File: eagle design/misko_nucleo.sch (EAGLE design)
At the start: 12 parts, among them U1 ESQ-119-24-T-D

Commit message: - removed arduino connectors from lib
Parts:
- removed TP10, TP9: TPPAD1-17, testpad:TPPAD1-17
- removed U1: ESQ-119-24-T-D, NUCLEO:NUCLEO-L053R8
- added C1: 18pF, rcl:C-EUC0805
- added C10, C14, C15, C9: 1µF, rcl:C-EUC0805
- added C11: 22µF, rcl:C-EUC0805
- added C12, C8: 7pF, resistor:C-EUC0805
- added C13, C20, C3, C41, C42: 0.1µF, resistor:C-EUC0805
- added C16, C29, C34, C6: 10µF, rcl:C-EUC0805
- added C17: 2.2µF / 25V, rcl:C-EUC0805
- added C18: 1nF, rcl:C-EUC0805
- added C19, C21, C32, C36, C4, C43, C45: 0.1µF, rcl:C-EUC0805
- added C2: 1µF, resistor:C-EUC0805
- added C23, C37, C5: 10µF, resistor:C-EUC0805
- added C25: 1.5F, EECS5R5H155 Supercap:EECS5R5H155
- added C27, C30, C31, C35, C38: 1000µF, rcl:CPOL-EUE5-10.5
- added C39, C40: 100µF, rcl:C-EUC0805
- added C7: 18pF, resistor:C-EUC0805
- added CONN1: JTAG, JTAG 1.27mm 10pin header:JTAG-1.27-10-PIN-HEADER
- added CONN2: I2C, jumper:JP4E
- added CONN3: LiPo Battery, SIM800C:JST_2PIN-THM-RA
- added CONN4: USB mini B, MX-67503-1230 USB Mini-B SMT straight socket:MX-67503-1230
- added D1: 1N4148, Diode2:1N4148
- added D2: BAT60AE6327, diode:BAT60J
- added D4: SZ1SMB5916BT3G, diode:DIODE-SMB
- added D7: BZG05C3V6-E3-TR3, zener:ZENER
- added F1: PTS120615V050, SparkFun-Fuses:PPTC_THREE-QUARTER-AMP
- added IC1: ATMEGA1281-16AU, Atmel_By_element14_Batch_1-00:ATMEGA1281-16AU
- added IC10: ORG1510-MK4, ORG1510-MK4 GPS module:ORG1510-MK4
- added IC11: TPS3808G33DBVT, Texas Instruments_By_element14_Batch_1:TPS3808G33DBVT
- added IC12: LTC4425, LTC4425 Supercap Charger:LTC4425
- added IC13: RN4678_BT_MODULE, RN4678 Bluetooth 4.2 Dual Mode:RN4678_BT_MODULE
- added IC14: ADXL345, ADXL345 Accelerometer:ADXL345
- added IC15: 74HCT1G32, 74HCT1G32GW:74HCT1G32GW-DC
- added IC16: FM25W256-SOIC, FM25W256 FERAM:FM25W256-SOIC
- added IC17: MICROSD_SPI_MODE, Molex SD-47309 SD Card Slot:MICROSD_SPI_MODE
- added IC18: FH12-30S-0.5SH, con-hirose:FH12-30S-0.5SH
- added IC19: DS1394U-33+, DS1394U-33+ RTC SPI Module:DS1394U-33+
- added IC2: MC1525TT, microchip:MC1525TT
- added IC23: SP3012-04UTG, SP3012 TVS Diode Array:SP3012-04UTG
- added IC3: TMP36GRTZ, TMP36GRTZ:TMP36GRTZ-REEL7
- added IC4: TPS63031, TPS63031 - Buck Boost Voltage Regulator:TPS63001DRCR
- added IC5: MCP73871-2AAI/ML, MCP73871 - Powerpath and Charge Controller:MCP73871-2AAI/ML
- added IC6: MAX6818, MAX6818 CMOS Switch debouncer:MAX6818
- added IC7: FT230XS, ftdichip:FT230XS
- added IC8: SN74LVC1G3157DBVR - BT switch, Texas Instruments_By_element14_Batch_1:SN74LVC1G3157DBVR
- added IC9: SN74LVC1G3157DBVR - GPS switch, Texas Instruments_By_element14_Batch_1:SN74LVC1G3157DBVR
- added L1: DL0805-33 33µH, rcl:L-US
- added L2: DJNR3015-1R5, DJNR3015-1R5 Inductor:DJNR3015-1R5
- added LED1: TX, led:LEDCHIPLED_1206
- added LED2: RX, led:LEDCHIPLED_1206
- added LED3: green, led:LEDSQR2X5
- added LED4: red, led:LEDSQR2X5
- added MISKO: misko, NUCLEO-H503RB-B02:NUCLEO-H503RB-B02
- added Q1: ABM3B-8MHZ-10-1-U-T, ABM3B-8MHZ-10-1-U-T - Quartz Resonator:ABM3B
- added Q2: LFXTAL016178R, LFXTAL016178R 32.768kHz crystal:LFXTAL016178R
- added R1, R16, R20, R25: 47k, rcl:R-EU_R0805
- added R10, R6: 27, resistor:R-EU_R0805
- added R12, R37: 100k, rcl:R-EU_R0805
- added R13, R39: 270k, rcl:R-EU_R0805
- added R14, R15, R22, R30, R35: 1k, resistor:R-EU_R0805
- added R17, R18, R33, R34: 1k, rcl:R-EU_R0805
- added R19, R32, R41, R9: 10k, rcl:R-EU_R0805
- added R2, R23, R27, R28, R36, R42, R43: 10k, resistor:R-EU_R0805
- added R26: 390k, rcl:R-EU_R0805
- added R29: 1M, resistor:R-EU_R0805
- added R3: 4k7, rcl:R-EU_R0805
- added R4, R5: 3k3, rcl:R-EU_R0805
- added R40: NTC 10k, rcl:R-EU_0204/5
- added R44, R45, R7, R8: 150k, rcl:R-EU_R0805
- added R46, R47: 470k, resistor:R-EU_R0805
- added SJ3: RESET, jumper:SJW
- added SW1: RESET, Wurth_Elektronik_Electromechanic_Switch_rev17c:430152050836
- added SW2: POWER SWITCH, smd-special:SWS001
- added SW3: MICROJOYSTICK, micro joystick:MICROJOYSTICK
- added SW4, SW5: PB6156RSL, PB6156RSL Illuminated Tact SPST-NO switch:PB6156RSL
- added T1: BSS84, transistor-small-signal:BSS84
- TP1, TP2, TP3: value TPPAD1-17 -> GND; device testpad:TPPAD1-17 -> testpad:TPPAD1-17Y
- TP11: value TPPAD1-17 -> Bluetooth Wakeup Pin; device testpad:TPPAD1-17 -> testpad:PTR1TP14R
- TP4: value TPPAD1-17 -> VCC; device testpad:TPPAD1-17 -> testpad:PTR1TP14R
- TP5: value TPPAD1-17 -> VLiIon Regulated; device testpad:TPPAD1-17 -> testpad:PTR1TP14R
- TP6: value TPPAD1-17 -> VGPS; device testpad:TPPAD1-17 -> testpad:PTR1TP14R
- TP7: value TPPAD1-17 -> Analogue Switch CRTL Pin; device testpad:TPPAD1-17 -> testpad:PTR1TP14R
- TP8: value TPPAD1-17 -> GPS Power CTRL Pin; device testpad:TPPAD1-17 -> testpad:PTR1B1,27
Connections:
- removed net 3V3: TP1.TP, TP7.TP, U1G$3.+3V3
- removed net AB-RTC_!INT!: TP6.TP
- removed net ANAL.SW.CTRL.: TP5.TP
- removed net EXTI_ADXL345: TP6.TP, U1G$6.PB4
- removed net EXTI_PUSHBUTTON: U1G$3.PC13
- removed net GPS_ON: TP1.TP
- removed net INT_AB-RTC: TP11.TP
- removed net LED_GREEN: U1G$3.PC10
- removed net LED_RED: U1G$3.PC11
- removed net N$2: TP4.TP
- removed net N$67: U1G$3.PA15
- removed net N$70: U1G$3.BOOT0
- removed net N$71: U1G$3.VDD
- removed net N$72: U1G$3.PC12
- removed net RCC_OSC_IN: U1G$3.PH0
- removed net SPI1_MISO: U1G$6.PA6
- removed net SPI1_MOSI: U1G$6.PA7
- removed net SPI1_SCK: U1G$6.PA5
- removed net SPI1_SS_ADXL345: U1G$6.PB6
- removed net SPI1_SS_MR25H256: U1G$6.PC7
- removed net SWCLK: U1G$3.PA14
- removed net SWDIO: U1G$3.PA13
- removed net USART2_RX: U1G$6.PA3
- removed net USART2_TX: U1G$6.PA2
- removed net USART3_RX: U1G$6.PB11
- removed net USART3_TX: U1G$6.PB10
- removed net USB_DM: U1G$6.PA11
- removed net USB_DP: U1G$6.PA12
- removed net VIN: TP9.TP, U1G$3.VIN
- removed net _AB-RTC_CLKOUT: TP5.TP
- removed net _GPS_1PPS: TP3.TP
- new net ADXL345SDA: IC14.SDA, IC15.Y
- new net ADXL345_INT1_INTERRUPT_PIN: CONN2.3, IC1.(SCL/INT0)_PD0, IC14.INT1
- new net ANALOG_SW_CTRL_PIN: IC1.PA7_(AD7), IC8.S, IC9.S, TP7.TP
- new net AREF: C5.1, IC1.AREF, IC2.VO
- new net AVCC: C41.2, IC1.AVCC, IC2.VIN, L1.2
- new net BAT_A_PIN: IC1.PF2_(ADC2), R44.2, R45.1
- new net BLUETOOTH_PROF_IND_PIN: IC1.PG2_(ALE), IC13.P0_5, TP11.TP
- new net BLUETOOTH_RX: IC13.RXD, IC8.A
- new net BLUETOOTH_SWITCH_PIN: IC1.PC6_(A14), IC13.SW_BTN, R43.2
- new net BLUETOOTH_TX: IC13.TXD, IC9.B1
- new net BLUETOOTH_WAKEUP_PIN: IC1.PC7_(A15), IC13.WAKEUP, R42.2
- new net BT_LED: IC13.LED, R22.1
- new net BUTTON_BLUETOOTH: IC6.IN7, SW4.3
- new net BUTTON_CENTER: IC6.IN5, SW3.CENTER
- new net BUTTON_DOWN: IC6.IN2, SW3.DOWN
- new net BUTTON_GPRS: IC6.IN8, SW5.3
- new net BUTTON_LEFT: IC6.IN4, SW3.LEFT
- new net BUTTON_RIGHT: IC6.IN3, SW3.RIGHT
- new net BUTTON_UP: IC6.IN6, SW3.UP
- new net CAP1N: C9.1, IC18-5.1
- new net CAP1P: C9.2, IC18-4.1
- new net CAP2N: C10.1, IC18-3.1
- new net CAP2P: C10.2, IC18-2.1
- new net CBUS1: IC7.CBUS1, LED2.C
- new net CBUS2: IC7.CBUS2, LED1.C
- new net D+: CONN4.D+, IC23.4
- new net D-: CONN4.D-, IC23.2
- new net EN: IC4.EN, R2.2, SW2.1
- new net GPRS_NETLIGHT: R27.1, R28.1
- new net GPRS_NETLIGHT_GATE: R28.2, T1.G
- new net GPS_GREEN_LED_PIN: IC1.PA3_(AD3), R17.1
- new net GPS_ON_OFF: IC10.ON_OFF, IC11.~RESET, R29.1
- new net GPS_POWER_CTL_PIN: IC1.PA6_(AD6), IC11.~MR, R23.1, TP8.TP
- new net GPS_RED_LED_PIN: IC1.PA4_(AD4), R18.1
- new net GPS_SW_SERIAL_RX: IC1.(OC2A/_PCINT4)_PB4, IC8.B2, IC9.A
- new net GPS_SW_SERIAL_TX: C7.2, IC1.(OC1A/PCINT5)_PB5, IC10.RX, IC8.B1
- new net GPS_TX: C1.1, IC10.TX, IC9.B2
- new net GPS_WAKEUP_PIN: IC1.PA5_(AD5), IC10.WAKEUP
- new net GREEN_LED: LED3.C, R17.2
- new net ID: CONN4.ID, IC23.5
- new net IREF: IC18-26.1, R26.2
- new net JTAG_TCL_PIN: CONN1.TCK, IC1.PF4_(ADC4/TCK)
- new net JTAG_TDI_PIN: CONN1.TDI, IC1.PF7_(ADC7/TDI)
- new net JTAG_TDO_PIN: CONN1.TDO, IC1.PF6_(ADC6/TDO)
- new net JTAG_TMS_PIN: CONN1.TMS, IC1.PF5_(ADC5/TMS)
- new net L2: R22.2, SW4.L2
- new net LDO33_O: IC13.LDO33_O, IC13.VDD_IO, SW4.L1
- new net LTC4425_EN: IC12.EN, R35.2
- new net LTC4425_PROG: IC12.PROG, R36.2
- new net L_L1: IC4.L1, L2.L1
- new net L_L2: IC4.L2, L2.L2
- new net MCP73871_CHARGE_STATUS_1_PIN: IC1.PA0_(AD0), IC5.STAT1/!LBO!, R25.2
- new net MCP73871_CHARGE_STATUS_2_PIN: IC1.PA1_(AD1), IC5.STAT2, R20.2
- new net MCP73871_POWER_GOOD_PIN: IC1.PA2_(AD2), IC5.!PG!, R16.2
- new net MENU_BLUETOOTH_POWER_BUTTON_PIN: IC1.PC4_(A12), IC6.OUT7
- new net MENU_CENTER_BUTTON_PIN: IC1.PC2_(A10), IC6.OUT5
- new net MENU_DOWN_BUTTON_PIN: IC1.PG1_(~RD), IC6.OUT2
- new net MENU_GPRS_POWER_BUTTON_PIN: IC1.PC5_(A13), IC6.OUT8
- new net MENU_LEFT_BUTTON_PIN: IC1.PC1_(A9), IC6.OUT4
- new net MENU_RIGHT_BUTTON_PIN: IC1.PC0_(A8), IC6.OUT3
- new net MENU_UP_BUTTON_PIN: IC1.PC3_(A11), IC6.OUT6
- new net N$12: MISKOCN7.5V0
- new net N$13: MISKOCN7.IOREF
- new net N$15: MISKOCN7.NRST
- new net N$16: MISKOCN7.BOOT0
- new net N$21: MISKOCN7.PD2
- new net N$22: MISKOCN7.PC15
- new net N$26: MISKOCN7.PC11
- new net N$27: MISKOCN7.PC10
- new net N$28: MISKOCN7.PC3
- new net N$31: C3.2, D1.A, R1.1
- new net N$32: MISKOCN7.PC0
- new net N$33: MISKOCN7.PB0
- new net N$34: MISKOCN7.PA15
- new net N$35: MISKOCN7.PA14
- new net N$4: F1.2, IC23.1
- new net N$46: MISKOCN10.PC8
- new net N$47: MISKOCN10.PC9
- new net N$48: MISKOCN10.AGND
- new net N$49: MISKOCN10.GND
- new net N$50: MISKOCN10.PA5
- new net N$53: MISKOCN10.PA10
- new net N$56: MISKOCN10.PB2
- new net N$6: C27.+, C30.+, C31.+, C35.+, C38.+, D2.C
- new net N$61: MISKOCN10.PB8
- new net N$64: MISKOCN10.PB13
- new net N$66: MISKOCN10.PB15
- new net PDI_UART0_CTS_PIN: IC1.(OC0B)_PG5, IC7.!CTS
- new net PDI_UART0_RX_PIN: IC1.(RXD0/PCINT8/PDI)_PE0, R4.1
- new net PDI_UART0_TX_PIN: IC1.(TXD0/PDO)_PE1, R5.1
- new net PFI: IC12.PFI, R46.1, R47.2
- new net PFI_RET: IC12.PFI_RET, R47.1
- new net PROG1: IC5.PROG1, R34.1
- new net PROG3: IC5.PROG3, R37.1
- new net RED_LED: LED4.C, R18.2
- new net RESET: CONN1.RESET, IC1.~RESET, R1.2, R3.2, SW1.2, SW1.4
- new net RTC_INT_INTERRUPT_PIN: CONN2.4, IC1.(SDA/INT1)_PD1, IC19.!INT!
- new net RTC_XTAL1: IC19.X1, Q2.XTAL1
- new net RTC_XTAL2: IC19.X2, Q2.XTAL2
- new net RXD: IC7.RXD, R5.2
- new net SD_CARD_DETECT_PIN: IC1.(XCK0/AIN0)_PE2, IC17.CARD_DETECT
- new net SPI_MISO_PIN: IC1.(MISO/PCINT3)_PB3, IC14.SDO, IC16.SO, IC17.DO, IC19.DOUT
- new net SPI_MOSI_PIN: IC1.(MOSI/PCINT2)_PB2, IC15.B, IC16.SI, IC17.DI, IC18-19.1, IC19.DIN
- new net SPI_OLED_D/C_PIN: IC1.(OC0A/OC1C/PCINT7)_PB7, IC18-15.1
- new net SPI_OLED_RESET_PIN: IC1.(TOSC2)_PG3, IC18-14.1
- new net SPI_SCK_PIN: IC1.(SCK/PCINT1)_PB1, IC14.SCL, IC16.SCK, IC17.CLK, IC18-18.1, IC19.SCLK
- new net SPI_SS_ADXL345_PIN: IC1.(OC1B/PCINT6)_PB6, IC14.!CS!, IC15.A, R9.2
- new net SPI_SS_FRAM_PIN: IC1.(~SS/PCINT0)_PB0, IC16.!CS!, R19.1
- new net SPI_SS_OLED_PIN: IC1.(TOSC1)_PG4, IC18-13.1
- new net SPI_SS_RTC_PIN: IC1.(OC3C/INT5)_PE5, IC19.!CS!, R32.2
- new net SPI_SS_SD_CARD_PIN: IC1.(OC3A/AIN1)_PE3, IC17.CS, R41.1
- new net THERM: IC5.THERM, R33.1
- new net TMP36_VSENSE_PIN: IC1.PF3_(ADC3), IC3.VOUT
- new net TXD: IC7.TXD, R4.2
- new net UART1_GPS_RX: IC1.(RXD1/INT2)_PD2
- new net UART1_GPS_TX: IC1.(TXD1/INT3)_PD3
- new net USBDM: IC7.USBDM, R10.1
- new net USBDP: IC7.USBDP, R6.2
- new net USB_D+: IC23.7, R6.1
- new net USB_D-: IC23.9, R10.2
- new net USB_ID: IC23.6
- new net USB_RX_LED: LED1.A, R14.2
- new net USB_TX_LED: LED2.A, R15.2
- new net VCC: C11.2, C14.2, C15.2, C16.2, C19.2, C20.1, C21.1, C29.1, C32.1, C34.1, C36.1, C4.1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
- new net VCC_SENSE_PIN: IC1.PF1_(ADC1), R7.2, R8.1
- new net VCOMH: C17.2, IC18-27.1
- new net VGPS: C18.1, C2.1, C25.+, C39.1, IC10.VCC, IC11.SENSE, IC12.VOUT1, IC12.VOUT2, IC19.VBACK, TP6.TP
- new net VMID: C39.2, C40.2, IC12.VMID
- new net VPCC: IC5.VPCC, R12.2, R13.1
- new net VUSB: CONN4.VBUS, F1.1, R14.1, R15.1, TP2.TP
- new net V_LIION+: C37.1, CONN3.2, IC5.VBAT1, IC5.VBAT2, IC5.VBAT_SENSE, R44.1
- new net V_LIION_REGULATED: C23.1, C45.1, C6.2, IC4.PS/SYNC, IC4.VIN, IC4.VINA, IC5.OUT1, IC5.OUT2, SW2.2, SW5.L1, TP5.TP
- new net XTAL1: C12.2, IC1.XTAL1, Q1.Q2
- new net XTAL2: C8.2, IC1.XTAL2, Q1.Q1
- net 5V0: now also C42.2, D2.A, IC23.10, IC5.!TE!, IC5.CE, IC5.IN1, IC5.IN2, IC5.PROG2, IC5.SEL, IC7.VCC, R12.1; no longer TP8.TP, U1G$3.+5V
- net GND: now also C1.2, C11.1, C12.1, C13.2, C14.1, C15.1, C16.1, C17.1, C18.2, C19.1, C2.2, C20.2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; no longer TP10.TP, U1G$3.GND_19, U1G$3.GND_20, U1G$3.GND_22, U1G$3.GND_8, U1G$6.GND_20, U1G$6.GND_9, U1G$7.GND_CN11_1, U1G$7.GND_CN11_2, U1G$7.GND_CN12_1, U1G$7.GND_CN12_2
- net N$1: now also R30.1, SW5.L2; no longer U1G$6.PC4
- net N$10: now also C13.1, IC7.!RESET, IC7.3V3OUT, IC7.VCCIO; no longer U1G$6.PB1
- net N$11: now also IC13.!RST_N!, SJ3.1; no longer U1G$6.PB2
- net N$14: now also MISKOCN7.3V3; no longer U1G$6.PB12
- net N$17: now also MISKOCN7.GND; no longer U1G$6.U5V
- net N$18: now also MISKOCN7.PF1; no longer U1G$6.PC5
- net N$19: now also R33.2, R39.1, R40.1; no longer U1G$6.PC6
- net N$20: now also MISKOCN7.PF0; no longer U1G$6.PC8
- net N$23: now also MISKOCN7.PC14; no longer U1G$6.PA10
- net N$24: now also MISKOCN7.PC13; no longer U1G$6.PB3
- net N$25: now also MISKOCN7.PC12; no longer U1G$6.PB5
- net N$29: now also MISKOCN7.PC2; no longer U1G$6.PA9
- net N$3: now also R30.2, T1.S; no longer TP3.TP
- net N$30: now also MISKOCN7.PC1; no longer U1G$6.PA8
- net N$36: now also MISKOCN7.PA13; no longer U1G$6.AVDD
- net N$37: now also MISKOCN7.PA2; no longer U1G$6.PB9
- net N$38: now also MISKOCN7.PA1; no longer U1G$6.PB8
- net N$39: now also MISKOCN7.PA0; no longer U1G$6.PC9
- net N$40: now also MISKOCN10.AVDD; no longer U1G$3.PC0
- net N$41: now also MISKOCN10.VBUS_STLK; no longer U1G$3.PC1
- net N$42: now also MISKOCN10.PC4; no longer U1G$3.PB0
- net N$43: now also MISKOCN10.PC5; no longer U1G$3.PA4
- net N$44: now also MISKOCN10.PC6; no longer U1G$3.PA1
- net N$45: now also MISKOCN10.PC7; no longer U1G$3.PA0
- net N$5: now also MISKOCN7.VBAT; no longer U1G$6.AGND
- net N$51: now also MISKOCN10.PA6; no longer U1G$3.RESET
- net N$52: now also MISKOCN10.PA7; no longer U1G$3.IOREF
- net N$54: now also MISKOCN10.PA8; no longer U1G$3.E5V
- net N$55: now also MISKOCN10.PB1; no longer U1G$3.PD2
- net N$57: now also MISKOCN10.PB4; no longer U1G$3.PC3
- net N$58: now also MISKOCN10.PB5; no longer U1G$3.PC2
- net N$59: now also MISKOCN10.PB6; no longer U1G$3.VLCD
- net N$60: now also MISKOCN10.PB7; no longer U1G$3.PH1
- net N$62: now also MISKOCN10.PB10; no longer U1G$3.PC15
- net N$63: now also MISKOCN10.PB12; no longer U1G$3.PC14
- net N$65: now also MISKOCN10.PB14; no longer U1G$3.PB7
- net N$7: now also MISKOCN7.VDD; no longer U1G$6.PB13
- net N$8: now also MISKOCN7.VIN; no longer U1G$6.PB14
- net N$9: now also MISKOCN7.E5V; no longer U1G$6.PB15
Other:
- note added: "ADXL345 Accelerometer"
- note added: "AVCC Circuit"
- note added: "Analog Switch"
- note added: "Bluetooth Module"
- note added: "Buttons"
- note added: "Debouncer"
- note added: "ER-OLED015-2W Connetor w. SSD1309"
- note added: "FERAM Module"
- note added: "GPS module"
- note added: "Joystick"
- note added: "Motherboard"
- note added: "OLED"
- note added: "Oscillator Circuit"
- note added: "Power Supply - Buck/Boost Regulator"
- note added: "Power Supply - Power Path Controller"
- note added: "RTC Clock"
- note added: "Reset Circuit"
- note added: "SD Card Slot"
- note added: "SPI Bus"
- note added: "Status LEDs"
- note added: "Supercap Charger"
- note added: "Temperature Sensor"
- note added: "USB connetor"
- note added: "USB to Serial"
- note added: "VGPS Voltage Supervisor"
- note added: "Vcc Measurement"
- note added: "Voltage Reference"
- note removed: "TODO: remove & hardwire"
- moved on the sheet: TP1, TP2, TP3

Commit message: - defined net classes, added power symbols, ground fill
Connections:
- net N$13 renamed IOREF
- net N$14 renamed 3V3
- net N$15 renamed NRST
- net N$16 renamed BOOT0
- net N$18 renamed PF1
- net N$20 renamed PF0
- net N$21 renamed PD2
- net N$22 renamed PC15
- net N$23 renamed PC14
- net N$24 renamed PC13
- net N$25 renamed PC12
- net N$26 renamed PC11
- net N$27 renamed PC10
- net N$28 renamed PC3
- net N$29 renamed PC2
- net N$30 renamed PC1
- net N$32 renamed PC0
- net N$33 renamed PB0
- net N$34 renamed PA15
- net N$35 renamed PA14
- net N$36 renamed PA13
- net N$37 renamed PA2
- net N$38 renamed PA1
- net N$39 renamed PA0
- net N$40 renamed AVDD
- net N$41 renamed VBUS_STLK
- net N$42 renamed PC4
- net N$43 renamed PC5
- net N$44 renamed PC6
- net N$45 renamed PC7
- net N$46 renamed PC8
- net N$47 renamed PC9
- net N$5 renamed VBAT
- net N$50 renamed PA5
- net N$51 renamed PA6
- net N$52 renamed PA7
- net N$53 renamed PA9
- net N$54 renamed PA8
- net N$55 renamed PB1
- net N$56 renamed PB2
- net N$57 renamed PB4
- net N$58 renamed PB5
- net N$59 renamed PB6
- net N$60 renamed PB7
- net N$61 renamed PB8
- net N$62 renamed PB10
- net N$63 renamed PN12
- net N$64 renamed PB13
- net N$65 renamed PB14
- net N$66 renamed PB15
- net N$7 renamed VDD
- net N$8 renamed VIN
- net N$9 renamed E5V
- removed net N$12: MISKOCN7.5V0
- removed net N$17: MISKOCN7.GND
- removed net N$48: MISKOCN10.AGND
- removed net N$49: MISKOCN10.GND
- new net OLD_5V0: C42.2, D2.A, IC23.10, IC5.!TE!, IC5.CE, IC5.IN1, IC5.IN2, IC5.PROG2, IC5.SEL, IC7.VCC, R12.1
- net 5V0: now also MISKOCN7.5V0; no longer C42.2, D2.A, IC23.10, IC5.!TE!, IC5.CE, IC5.IN1, IC5.IN2, IC5.PROG2, IC5.SEL, IC7.VCC, R12.1
- net GND: now also MISKOCN10.AGND, MISKOCN10.GND, MISKOCN7.GND

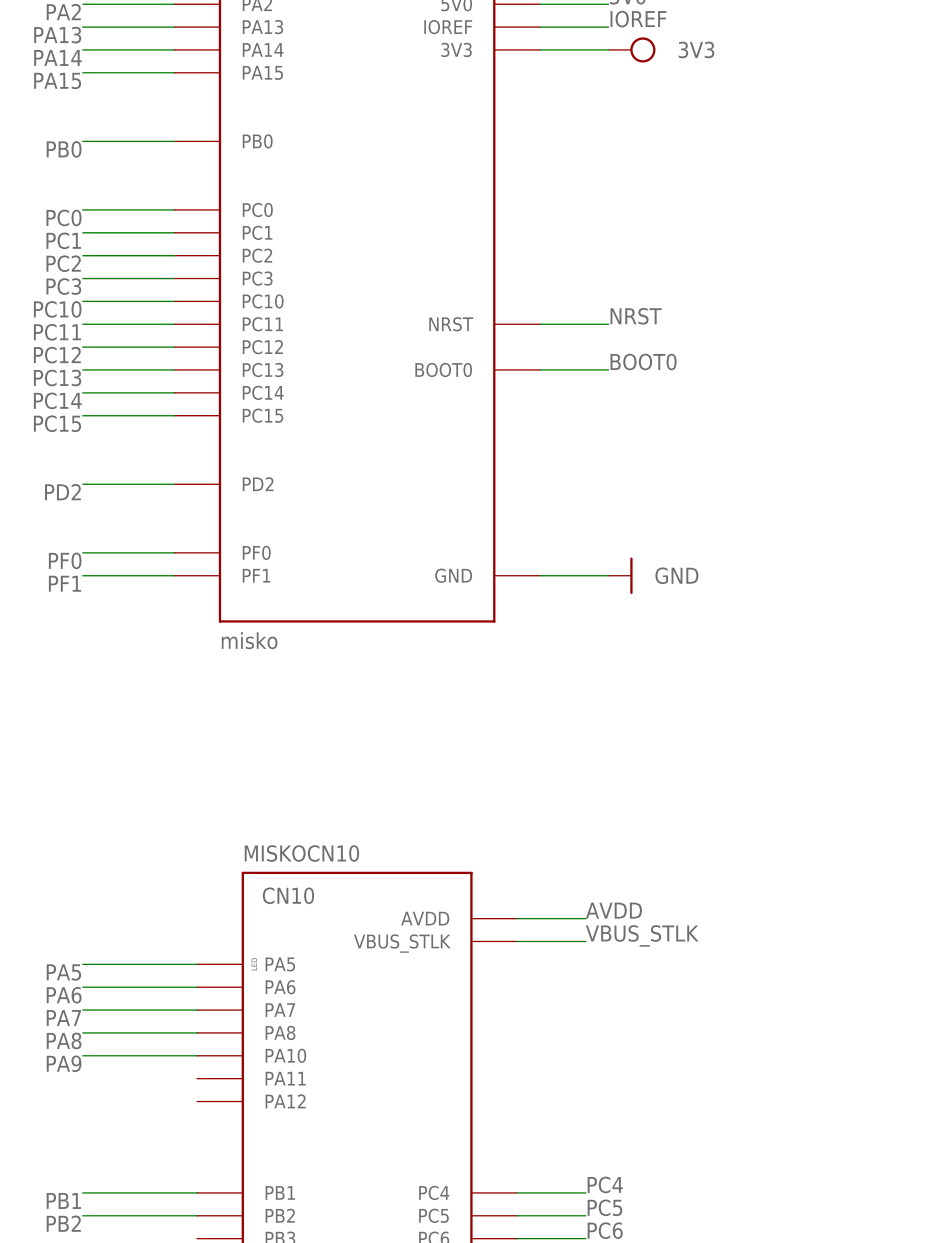
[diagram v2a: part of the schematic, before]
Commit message: - annotated key peripherals to documentation layer - named nets for pin indentification
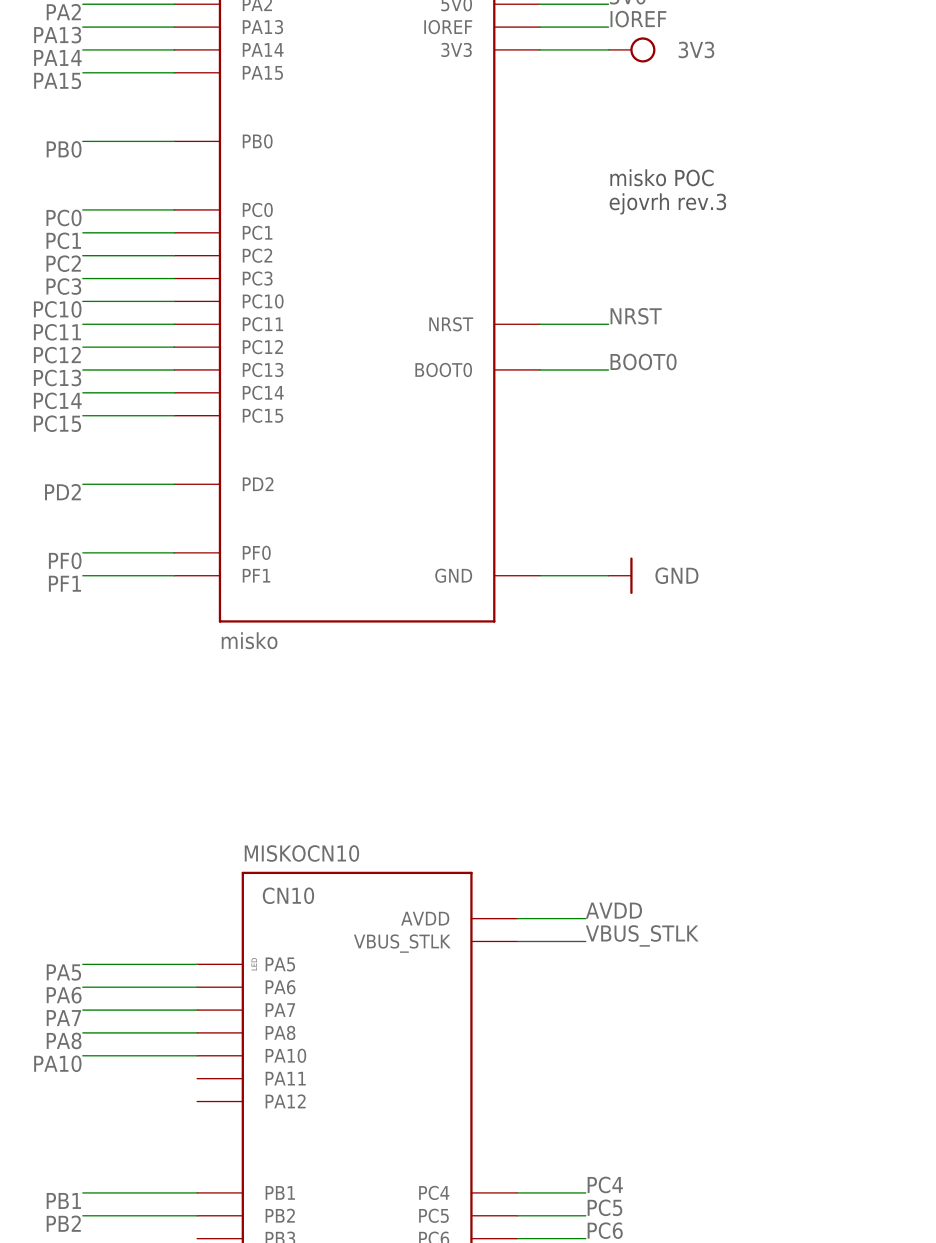
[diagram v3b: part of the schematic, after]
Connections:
- net PA9 renamed PA10
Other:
- note added: "misko POC ejovrh rev.3"
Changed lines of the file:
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@@
 <setting verticaltext="up"/>
 </settings>
-<grid distance="0.1" unitdist="inch" unit="inch" style="dots" multiple="1" display="yes" altdistance="0.01" altunitdist="inch" altunit="inch"/>
+<grid distance="0.1" unitdist="inch" unit="inch" style="lines" multiple="1" display="no" altdistance="0.01" altunitdist="inch" altunit="inch"/>
 <layers>
 <layer number="1" name="Top" color="4" fill="1" visible="no" active="no"/>
@@
 <part name="SUPPLY5" library="Power_Symbols" library_urn="urn:adsk.eagle:library:16502351" deviceset="GND-BAR" device="" value="GND"/>
 <part name="SUPPLY6" library="Power_Symbols" library_urn="urn:adsk.eagle:library:16502351" deviceset="GND-BAR" device="" value="GND"/>
+<part name="MISKO-POC" library="frames" library_urn="urn:adsk.eagle:library:229" deviceset="A3L-LOC" device="" value="misko POC, rev.3"/>
 </parts>
 <sheets>
@@
 <text x="243.84" y="266.7" size="1.778" layer="97">USB connetor</text>
 <text x="124.46" y="93.98" size="1.778" layer="97">VGPS Voltage Supervisor</text>
+<text x="-429.26" y="662.94" size="1.778" layer="97">misko POC
+ejovrh rev.3</text>
 </plain>
 <instances>
@@
 <attribute name="VALUE" x="-424.18" y="622.3" size="1.778" layer="96" align="center-left"/>
 </instance>
+<instance part="MISKO-POC" gate="G$1" x="-513.08" y="480.06" smashed="yes">
+<attribute name="DRAWING_NAME" x="-168.91" y="495.3" size="2.54" layer="94"/>
+<attribute name="LAST_DATE_TIME" x="-168.91" y="490.22" size="2.286" layer="94"/>
+<attribute name="SHEET" x="-155.575" y="485.14" size="2.54" layer="94"/>
+</instance>
 </instances>
 <busses>
@@
 </segment>
 </net>
-<net name="PA9" class="2">
+<net name="PA10" class="2">
 <segment>
 <wire x1="-474.98" y1="568.96" x2="-487.68" y2="568.96" width="0.1524" layer="91"/>
@@
 </drawing>
 <compatibility>
+<note version="6.3" minversion="6.2.2" severity="warning">
+Since Version 6.2.2 text objects can contain more than one line,
+which will not be processed correctly with this version.
+</note>
 <note version="8.2" severity="warning">
 Since Version 8.2, EAGLE supports online libraries. The ids

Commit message: - defined and connected legacy board GPIOs
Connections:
- net PA0 renamed ADC_VGPS
- net PA10 renamed GPS_WKUP
- net PA6 renamed SPI_FRAM_CS
- net PA7 renamed ADXL345_CS
- net PA8 renamed SPI1_SCK
- net PB14 renamed UART1_TX
- net PB15 renamed UART1_RX
- net PB4 renamed SPI1_MISO
- net PB5 renamed SPI1_MOSI
- net PB8 renamed ANAL_SW_CTRL
- net PC11 renamed GPS_GREEN_LED
- net PC12 renamed GPS_RED_LED
- net PC4 renamed GPS_PWR_CTRL
- net PC6 renamed CAN_RX
- net PC7 renamed CAN_TX
- net PC8 renamed DEBUG_OUT
- net PC9 renamed ADXL345_INT
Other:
- moved on the sheet: C1, C10, C11, C12, C13, C14, C15, C16, C17, C18, C19, C2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

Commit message: - added ADXL345 module to schematic
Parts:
- removed C39, C40: 100µF, rcl:C-EUC0805
- removed C41, C42: 0.1µF, resistor:C-EUC0805
- removed C43, C45: 0.1µF, rcl:C-EUC0805
- removed CONN3: LiPo Battery, SIM800C:JST_2PIN-THM-RA
- removed CONN4: USB mini B, MX-67503-1230 USB Mini-B SMT straight socket:MX-67503-1230
- removed D7: BZG05C3V6-E3-TR3, zener:ZENER
- removed IC12: LTC4425, LTC4425 Supercap Charger:LTC4425
- removed IC13: RN4678_BT_MODULE, RN4678 Bluetooth 4.2 Dual Mode:RN4678_BT_MODULE
- removed IC14: ADXL345, ADXL345 Accelerometer:ADXL345
- removed IC15: 74HCT1G32, 74HCT1G32GW:74HCT1G32GW-DC
- removed IC16: FM25W256-SOIC, FM25W256 FERAM:FM25W256-SOIC
- removed IC17: MICROSD_SPI_MODE, Molex SD-47309 SD Card Slot:MICROSD_SPI_MODE
- removed IC18: FH12-30S-0.5SH, con-hirose:FH12-30S-0.5SH
- removed IC19: DS1394U-33+, DS1394U-33+ RTC SPI Module:DS1394U-33+
- removed IC23: SP3012-04UTG, SP3012 TVS Diode Array:SP3012-04UTG
- removed MISKO: misko, NUCLEO-H503RB-B02:NUCLEO-H503RB-B02
- removed R42, R43: 10k, resistor:R-EU_R0805
- removed R44, R45: 150k, rcl:R-EU_R0805
- removed R46, R47: 470k, resistor:R-EU_R0805
- removed SJ3: RESET, jumper:SJW
- removed SW4, SW5: PB6156RSL, PB6156RSL Illuminated Tact SPST-NO switch:PB6156RSL
- removed T1: BSS84, transistor-small-signal:BSS84
- added BRD1: misko, NUCLEO-H503RB-B02:NUCLEO-H503RB-B02
- added C22, C28: 0.1µF, rcl:C-EUC0805
- added C24: 1.5F, EECS5R5H155 Supercap:EECS5R5H155
- added C26, C33: 1000µF, rcl:CPOL-EUE5-10.5
- added CN1: LiPo Battery, SIM800C:JST_2PIN-THM-RA
- added D3: SZ1SMB5916BT3G, diode:DIODE-SMB
- added JP1: I2C, jumper:JP4E
- added Q3: LFXTAL016178R, LFXTAL016178R 32.768kHz crystal:LFXTAL016178R
- added R11: 270k, rcl:R-EU_R0805
- added R21: 47k, rcl:R-EU_R0805
- added R24: 10k, resistor:R-EU_R0805
- added R31: 1k, rcl:R-EU_R0805
- added R38: 150k, rcl:R-EU_R0805
- added S1: RESET, Wurth_Elektronik_Electromechanic_Switch_rev17c:430152050836
- added S2: POWER SWITCH, smd-special:SWS001
- added SJ1: RESET, jumper:SJW
- added U1: SN74LVC1G3157DBVR - BT switch, Texas Instruments_By_element14_Batch_1:SN74LVC1G3157DBVR
- added U2: ATMEGA1281-16AU, Atmel_By_element14_Batch_1-00:ATMEGA1281-16AU
- added U3: TPS3808G33DBVT, Texas Instruments_By_element14_Batch_1:TPS3808G33DBVT
- added U4: TMP36GRTZ, TMP36GRTZ:TMP36GRTZ-REEL7
- added U5: MCP73871-2AAI/ML, MCP73871 - Powerpath and Charge Controller:MCP73871-2AAI/ML
- added U6: SN74LVC1G3157DBVR - GPS switch, Texas Instruments_By_element14_Batch_1:SN74LVC1G3157DBVR
- added X1: FH12-30S-0.5SH, con-hirose:FH12-30S-0.5SH
- C19: value 0.1µF -> 10µF
- C20, C5: device resistor:C-EUC0805 -> rcl:C-EUC0805
- C21, C36: device rcl:C-EUC0805 -> resistor:C-EUC0805
- C25: value 1.5F -> 1000µF; device EECS5R5H155 Supercap:EECS5R5H155 -> rcl:CPOL-EUE5-10.5
- C31, C38: value 1000µF -> 0.1µF; device rcl:CPOL-EUE5-10.5 -> rcl:C-EUC0805
- C32, C4: value 0.1µF -> 10µF; device rcl:C-EUC0805 -> resistor:C-EUC0805
- C34: value 10µF -> 100µF
- C35: value 1000µF -> 100µF; device rcl:CPOL-EUE5-10.5 -> rcl:C-EUC0805
- C37, C6: value 10µF -> 0.1µF
- CONN1: value JTAG -> USB mini B; device JTAG 1.27mm 10pin header:JTAG-1.27-10-PIN-HEADER -> MX-67503-1230 USB Mini-B SMT straight socket:MX-67503-1230
- CONN2: value I2C -> JTAG; device jumper:JP4E -> JTAG 1.27mm 10pin header:JTAG-1.27-10-PIN-HEADER
- D2: value BAT60AE6327 -> BZG05C3V6-E3-TR3; device diode:BAT60J -> zener:ZENER
- D4: value SZ1SMB5916BT3G -> BAT60AE6327; device diode:DIODE-SMB -> diode:BAT60J
- IC1: value ATMEGA1281-16AU -> MC1525TT; device Atmel_By_element14_Batch_1-00:ATMEGA1281-16AU -> microchip:MC1525TT
- IC10: value ORG1510-MK4 -> LTC4425; device ORG1510-MK4 GPS module:ORG1510-MK4 -> LTC4425 Supercap Charger:LTC4425
- IC11: value TPS3808G33DBVT -> SP3012-04UTG; device Texas Instruments_By_element14_Batch_1:TPS3808G33DBVT -> SP3012 TVS Diode Array:SP3012-04UTG
- IC2: value MC1525TT -> ORG1510-MK4; device microchip:MC1525TT -> ORG1510-MK4 GPS module:ORG1510-MK4
- IC3: value TMP36GRTZ -> TPS63031; device TMP36GRTZ:TMP36GRTZ-REEL7 -> TPS63031 - Buck Boost Voltage Regulator:TPS63001DRCR
- IC4: value TPS63031 -> FT230XS; device TPS63031 - Buck Boost Voltage Regulator:TPS63001DRCR -> ftdichip:FT230XS
- IC5: value MCP73871-2AAI/ML -> RN4678_BT_MODULE; device MCP73871 - Powerpath and Charge Controller:MCP73871-2AAI/ML -> RN4678 Bluetooth 4.2 Dual Mode:RN4678_BT_MODULE
- IC6: value MAX6818 -> FM25W256-SOIC; device MAX6818 CMOS Switch debouncer:MAX6818 -> FM25W256 FERAM:FM25W256-SOIC
- IC7: value FT230XS -> MICROSD_SPI_MODE; device ftdichip:FT230XS -> Molex SD-47309 SD Card Slot:MICROSD_SPI_MODE
- IC8: value SN74LVC1G3157DBVR - BT switch -> DS1394U-33+; device Texas Instruments_By_element14_Batch_1:SN74LVC1G3157DBVR -> DS1394U-33+ RTC SPI Module:DS1394U-33+
- IC9: value SN74LVC1G3157DBVR - GPS switch -> MAX6818; device Texas Instruments_By_element14_Batch_1:SN74LVC1G3157DBVR -> MAX6818 CMOS Switch debouncer:MAX6818
- L1: value DL0805-33 33µH -> DJNR3015-1R5; device rcl:L-US -> DJNR3015-1R5 Inductor:DJNR3015-1R5
- L2: value DJNR3015-1R5 -> DL0805-33 33µH; device DJNR3015-1R5 Inductor:DJNR3015-1R5 -> rcl:L-US
- Q2: value LFXTAL016178R -> BSS84; device LFXTAL016178R 32.768kHz crystal:LFXTAL016178R -> transistor-small-signal:BSS84
- R10: value 27 -> 100k; device resistor:R-EU_R0805 -> rcl:R-EU_R0805
- R12: value 100k -> 1k; device rcl:R-EU_R0805 -> resistor:R-EU_R0805
- R13: value 270k -> 1k; device rcl:R-EU_R0805 -> resistor:R-EU_R0805
- R14, R18: value 1k -> 10k
- R15: value 1k -> 47k; device resistor:R-EU_R0805 -> rcl:R-EU_R0805
- R16: value 47k -> 1k
- R19: value 10k -> 47k
- R20, R25: value 47k -> 1k; device rcl:R-EU_R0805 -> resistor:R-EU_R0805
- R22: value 1k -> 390k; device resistor:R-EU_R0805 -> rcl:R-EU_R0805
- R26: value 390k -> 1M; device rcl:R-EU_R0805 -> resistor:R-EU_R0805
- R29: value 1M -> 10k; device resistor:R-EU_R0805 -> rcl:R-EU_R0805
- R30: device resistor:R-EU_R0805 -> rcl:R-EU_R0805
- R32: value 10k -> 1k; device rcl:R-EU_R0805 -> resistor:R-EU_R0805
- R33: value 1k -> 10k; device rcl:R-EU_R0805 -> resistor:R-EU_R0805
- R34: value 1k -> 100k
- R35: value 1k -> 270k; device resistor:R-EU_R0805 -> rcl:R-EU_R0805
- R36: value 10k -> NTC 10k; device resistor:R-EU_R0805 -> rcl:R-EU_0204/5
- R37: value 100k -> 10k
- R39: value 270k -> 150k
- R40: value NTC 10k -> 470k; device rcl:R-EU_0204/5 -> resistor:R-EU_R0805
- R41: value 10k -> 470k; device rcl:R-EU_R0805 -> resistor:R-EU_R0805
- R9: value 10k -> 27; device rcl:R-EU_R0805 -> resistor:R-EU_R0805
- SW1: value RESET -> MICROJOYSTICK; device Wurth_Elektronik_Electromechanic_Switch_rev17c:430152050836 -> micro joystick:MICROJOYSTICK
- SW2: value POWER SWITCH -> PB6156RSL; device smd-special:SWS001 -> PB6156RSL Illuminated Tact SPST-NO switch:PB6156RSL
- SW3: value MICROJOYSTICK -> PB6156RSL; device micro joystick:MICROJOYSTICK -> PB6156RSL Illuminated Tact SPST-NO switch:PB6156RSL
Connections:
- removed net ADXL345_INT: MISKOCN10.PC9
- new net ADXL345_INT1: BRD1CN10.PC9, IC1.INT1
- new net ADXL345_INT2: IC1.INT2
- net 3V3: now also BRD1CN7.3V3, C4.1, IC1.VDDIO, IC1.VS, IC2.VCC, R1.2; no longer MISKOCN7.3V3
- net 5V0: now also BRD1CN7.5V0; no longer MISKOCN7.5V0
- net ADC_VGPS: now also BRD1CN7.PA0; no longer MISKOCN7.PA0
- net ADXL345SDA: now also IC1.SDA, IC2.Y; no longer IC14.SDA, IC15.Y
- net ADXL345_CS: now also BRD1CN10.PA7, IC1.!CS!, IC2.A, R1.1; no longer MISKOCN10.PA7
- net ADXL345_INT1_INTERRUPT_PIN: now also JP1.3, U2.(SCL/INT0)_PD0; no longer CONN2.3, IC1.(SCL/INT0)_PD0, IC14.INT1
- net ANALOG_SW_CTRL_PIN: now also U1.S, U2.PA7_(AD7), U6.S; no longer IC1.PA7_(AD7), IC8.S, IC9.S
- net ANAL_SW_CTRL: now also BRD1CN10.PB8; no longer MISKOCN10.PB8
- net AREF: now also C4.1, IC1.VO, U2.AREF; no longer C5.1, IC1.AREF, IC2.VO
- net AVCC: now also C36.2, IC1.VIN, L2.2, U2.AVCC; no longer C41.2, IC1.AVCC, IC2.VIN, L1.2
- net AVDD: now also BRD1CN10.AVDD; no longer MISKOCN10.AVDD
- net BAT_A_PIN: now also R38.2, R39.1, U2.PF2_(ADC2); no longer IC1.PF2_(ADC2), R44.2, R45.1
- net BLUETOOTH_PROF_IND_PIN: now also IC5.P0_5, U2.PG2_(ALE); no longer IC1.PG2_(ALE), IC13.P0_5
- net BLUETOOTH_RX: now also IC5.RXD, U1.A; no longer IC13.RXD, IC8.A
- net BLUETOOTH_SWITCH_PIN: now also IC5.SW_BTN, R28.2, U2.PC6_(A14); no longer IC1.PC6_(A14), IC13.SW_BTN, R43.2
- net BLUETOOTH_TX: now also IC5.TXD, U6.B1; no longer IC13.TXD, IC9.B1
- net BLUETOOTH_WAKEUP_PIN: now also IC5.WAKEUP, R27.2, U2.PC7_(A15); no longer IC1.PC7_(A15), IC13.WAKEUP, R42.2
- net BOOT0: now also BRD1CN7.BOOT0; no longer MISKOCN7.BOOT0
- net BT_LED: now also IC5.LED, R20.1; no longer IC13.LED, R22.1
- net BUTTON_BLUETOOTH: now also IC9.IN7, SW3.3; no longer IC6.IN7, SW4.3
- net BUTTON_CENTER: now also IC9.IN5, SW1.CENTER; no longer IC6.IN5, SW3.CENTER
- net BUTTON_DOWN: now also IC9.IN2, SW1.DOWN; no longer IC6.IN2, SW3.DOWN
- net BUTTON_GPRS: now also IC9.IN8, SW2.3; no longer IC6.IN8, SW5.3
- net BUTTON_LEFT: now also IC9.IN4, SW1.LEFT; no longer IC6.IN4, SW3.LEFT
- net BUTTON_RIGHT: now also IC9.IN3, SW1.RIGHT; no longer IC6.IN3, SW3.RIGHT
- net BUTTON_UP: now also IC9.IN6, SW1.UP; no longer IC6.IN6, SW3.UP
- net CAN_RX: now also BRD1CN10.PC6; no longer MISKOCN10.PC6
- net CAN_TX: now also BRD1CN10.PC7; no longer MISKOCN10.PC7
- net CAP1N: now also X1-5.1; no longer IC18-5.1
- net CAP1P: now also X1-4.1; no longer IC18-4.1
- net CAP2N: now also X1-3.1; no longer IC18-3.1
- net CAP2P: now also X1-2.1; no longer IC18-2.1
- net CBUS1: now also IC4.CBUS1; no longer IC7.CBUS1
- net CBUS2: now also IC4.CBUS2; no longer IC7.CBUS2
- net D+: now also CONN1.D+, IC11.4; no longer CONN4.D+, IC23.4
- net D-: now also CONN1.D-, IC11.2; no longer CONN4.D-, IC23.2
- net DEBUG_OUT: now also BRD1CN10.PC8; no longer MISKOCN10.PC8
- net E5V: now also BRD1CN7.E5V; no longer MISKOCN7.E5V
- net EN: now also IC3.EN, S2.1; no longer IC4.EN, SW2.1
- net GND: now also BRD1CN10.AGND, BRD1CN10.GND, BRD1CN7.GND, C19.2, C20.1, C22.2, C24.-, C26.-, C28.2, C31.2, C33.-, C35.1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; no longer C19.1, C20.2, C31.-, C34.2, C35.-, C36.2, C37.2, C38.-, C40.1, C41.1, C42.1, C43.1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
- net GPRS_NETLIGHT: now also R23.1, R24.1; no longer R27.1, R28.1
- net GPRS_NETLIGHT_GATE: now also Q2.G, R24.2; no longer R28.2, T1.G
- net GPS_GREEN_LED: now also BRD1CN7.PC11; no longer MISKOCN7.PC11
- net GPS_GREEN_LED_PIN: now also R16.1, U2.PA3_(AD3); no longer IC1.PA3_(AD3), R17.1
- net GPS_ON_OFF: now also IC2.ON_OFF, R26.1, U3.~RESET; no longer IC10.ON_OFF, IC11.~RESET, R29.1
- net GPS_POWER_CTL_PIN: now also R14.1, U2.PA6_(AD6), U3.~MR; no longer IC1.PA6_(AD6), IC11.~MR, R23.1
- net GPS_PWR_CTRL: now also BRD1CN10.PC4; no longer MISKOCN10.PC4
- net GPS_RED_LED: now also BRD1CN7.PC12; no longer MISKOCN7.PC12
- net GPS_RED_LED_PIN: now also R17.1, U2.PA4_(AD4); no longer IC1.PA4_(AD4), R18.1
- net GPS_SW_SERIAL_RX: now also U1.B2, U2.(OC2A/_PCINT4)_PB4, U6.A; no longer IC1.(OC2A/_PCINT4)_PB4, IC8.B2, IC9.A
- net GPS_SW_SERIAL_TX: now also IC2.RX, U1.B1, U2.(OC1A/PCINT5)_PB5; no longer IC1.(OC1A/PCINT5)_PB5, IC10.RX, IC8.B1
- net GPS_TX: now also IC2.TX, U6.B2; no longer IC10.TX, IC9.B2
- net GPS_WAKEUP_PIN: now also IC2.WAKEUP, U2.PA5_(AD5); no longer IC1.PA5_(AD5), IC10.WAKEUP
- net GPS_WKUP: now also BRD1CN10.PA10; no longer MISKOCN10.PA10
- net GREEN_LED: now also R16.2; no longer R17.2
- net ID: now also CONN1.ID, IC11.5; no longer CONN4.ID, IC23.5
- net IOREF: now also BRD1CN7.IOREF; no longer MISKOCN7.IOREF
- net IREF: now also R22.2, X1-26.1; no longer IC18-26.1, R26.2
- net JTAG_TCL_PIN: now also CONN2.TCK, U2.PF4_(ADC4/TCK); no longer CONN1.TCK, IC1.PF4_(ADC4/TCK)
- net JTAG_TDI_PIN: now also CONN2.TDI, U2.PF7_(ADC7/TDI); no longer CONN1.TDI, IC1.PF7_(ADC7/TDI)
- net JTAG_TDO_PIN: now also CONN2.TDO, U2.PF6_(ADC6/TDO); no longer CONN1.TDO, IC1.PF6_(ADC6/TDO)
- net JTAG_TMS_PIN: now also CONN2.TMS, U2.PF5_(ADC5/TMS); no longer CONN1.TMS, IC1.PF5_(ADC5/TMS)
- net L2: now also R20.2, SW3.L2; no longer R22.2, SW4.L2
- net LDO33_O: now also IC5.LDO33_O, IC5.VDD_IO, SW3.L1; no longer IC13.LDO33_O, IC13.VDD_IO, SW4.L1
- net LTC4425_EN: now also IC10.EN, R32.2; no longer IC12.EN, R35.2
- net LTC4425_PROG: now also IC10.PROG, R33.2; no longer IC12.PROG, R36.2
- net L_L1: now also IC3.L1, L1.L1; no longer IC4.L1, L2.L1
- net L_L2: now also IC3.L2, L1.L2; no longer IC4.L2, L2.L2
- net MCP73871_CHARGE_STATUS_1_PIN: now also R21.2, U2.PA0_(AD0), U5.STAT1/!LBO!; no longer IC1.PA0_(AD0), IC5.STAT1/!LBO!, R25.2
- net MCP73871_CHARGE_STATUS_2_PIN: now also R19.2, U2.PA1_(AD1), U5.STAT2; no longer IC1.PA1_(AD1), IC5.STAT2, R20.2
- net MCP73871_POWER_GOOD_PIN: now also R15.2, U2.PA2_(AD2), U5.!PG!; no longer IC1.PA2_(AD2), IC5.!PG!, R16.2
- net MENU_BLUETOOTH_POWER_BUTTON_PIN: now also IC9.OUT7, U2.PC4_(A12); no longer IC1.PC4_(A12), IC6.OUT7
- net MENU_CENTER_BUTTON_PIN: now also IC9.OUT5, U2.PC2_(A10); no longer IC1.PC2_(A10), IC6.OUT5
- net MENU_DOWN_BUTTON_PIN: now also IC9.OUT2, U2.PG1_(~RD); no longer IC1.PG1_(~RD), IC6.OUT2
- net MENU_GPRS_POWER_BUTTON_PIN: now also IC9.OUT8, U2.PC5_(A13); no longer IC1.PC5_(A13), IC6.OUT8
- net MENU_LEFT_BUTTON_PIN: now also IC9.OUT4, U2.PC1_(A9); no longer IC1.PC1_(A9), IC6.OUT4
- net MENU_RIGHT_BUTTON_PIN: now also IC9.OUT3, U2.PC0_(A8); no longer IC1.PC0_(A8), IC6.OUT3
- net MENU_UP_BUTTON_PIN: now also IC9.OUT6, U2.PC3_(A11); no longer IC1.PC3_(A11), IC6.OUT6
- net N$1: now also R25.1, SW2.L2; no longer R30.1, SW5.L2
- net N$10: now also IC4.!RESET, IC4.3V3OUT, IC4.VCCIO; no longer IC7.!RESET, IC7.3V3OUT, IC7.VCCIO
- net N$11: now also IC5.!RST_N!, SJ1.1; no longer IC13.!RST_N!, SJ3.1
- net N$19: now also R30.2, R35.1, R36.1; no longer R33.2, R39.1, R40.1
- net N$3: now also Q2.S, R25.2; no longer R30.2, T1.S
- net N$4: now also IC11.1; no longer IC23.1
- net N$6: now also C25.+, C26.+, C33.+, D4.C; no longer C31.+, C35.+, C38.+, D2.C
- net NRST: now also BRD1CN7.NRST; no longer MISKOCN7.NRST
- net OLD_5V0: now also C37.2, D4.A, IC11.10, IC4.VCC, R10.1, U5.!TE!, U5.CE, U5.IN1, U5.IN2, U5.PROG2, U5.SEL; no longer C42.2, D2.A, IC23.10, IC5.!TE!, IC5.CE, IC5.IN1, IC5.IN2, IC5.PROG2, IC5.SEL, IC7.VCC, R12.1
- net PA1: now also BRD1CN7.PA1; no longer MISKOCN7.PA1
- net PA13: now also BRD1CN7.PA13; no longer MISKOCN7.PA13
- net PA14: now also BRD1CN7.PA14; no longer MISKOCN7.PA14
- net PA15: now also BRD1CN7.PA15; no longer MISKOCN7.PA15
- net PA2: now also BRD1CN7.PA2; no longer MISKOCN7.PA2
- net PA5: now also BRD1CN10.PA5; no longer MISKOCN10.PA5
- net PB0: now also BRD1CN7.PB0; no longer MISKOCN7.PB0
- net PB1: now also BRD1CN10.PB1; no longer MISKOCN10.PB1
- net PB10: now also BRD1CN10.PB10; no longer MISKOCN10.PB10
- net PB13: now also BRD1CN10.PB13; no longer MISKOCN10.PB13
- net PB2: now also BRD1CN10.PB2; no longer MISKOCN10.PB2
- net PB6: now also BRD1CN10.PB6; no longer MISKOCN10.PB6
- net PB7: now also BRD1CN10.PB7; no longer MISKOCN10.PB7
- net PC0: now also BRD1CN7.PC0; no longer MISKOCN7.PC0
- net PC1: now also BRD1CN7.PC1; no longer MISKOCN7.PC1
- net PC10: now also BRD1CN7.PC10; no longer MISKOCN7.PC10
- net PC13: now also BRD1CN7.PC13; no longer MISKOCN7.PC13
- net PC14: now also BRD1CN7.PC14; no longer MISKOCN7.PC14
- net PC15: now also BRD1CN7.PC15; no longer MISKOCN7.PC15
- net PC2: now also BRD1CN7.PC2; no longer MISKOCN7.PC2
- net PC3: now also BRD1CN7.PC3; no longer MISKOCN7.PC3
- net PC5: now also BRD1CN10.PC5; no longer MISKOCN10.PC5
- net PD2: now also BRD1CN7.PD2; no longer MISKOCN7.PD2
- net PDI_UART0_CTS_PIN: now also IC4.!CTS, U2.(OC0B)_PG5; no longer IC1.(OC0B)_PG5, IC7.!CTS
- net PDI_UART0_RX_PIN: now also U2.(RXD0/PCINT8/PDI)_PE0; no longer IC1.(RXD0/PCINT8/PDI)_PE0
- net PDI_UART0_TX_PIN: now also U2.(TXD0/PDO)_PE1; no longer IC1.(TXD0/PDO)_PE1
- net PF0: now also BRD1CN7.PF0; no longer MISKOCN7.PF0
- net PF1: now also BRD1CN7.PF1; no longer MISKOCN7.PF1
- net PFI: now also IC10.PFI, R40.1, R41.2; no longer IC12.PFI, R46.1, R47.2
- net PFI_RET: now also IC10.PFI_RET, R41.1; no longer IC12.PFI_RET, R47.1
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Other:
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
